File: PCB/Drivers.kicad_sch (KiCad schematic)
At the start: 95 parts, among them U10 TMC2209-LA-T, U11 TMC2209-LA-T, U5 TMC2209-LA-T, U6 ISO1042DWVR, U7 TMC2209-LA-T, U8 TMC2209-LA-T, U9 TMC2209-LA-T

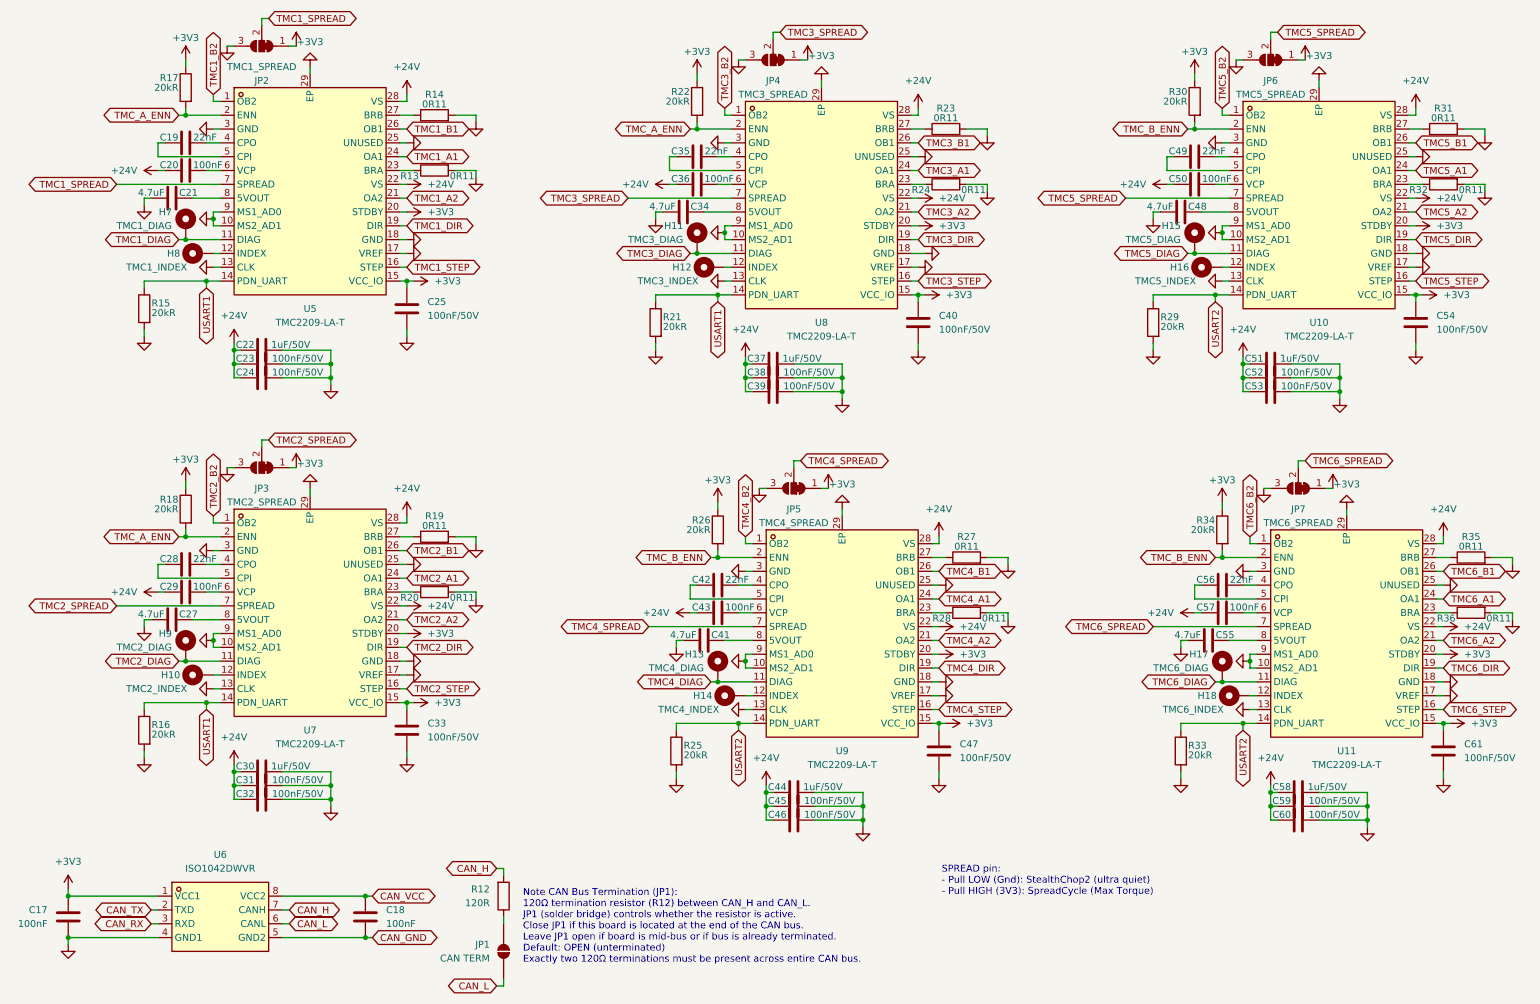
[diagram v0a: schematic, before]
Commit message: Improved Protection and Board Testability - Added power rail protection and decoupling for stepper motor noise environment - Added TVS, bulk caps and fuse upgrade on 24V rail - Added test pads for bring-up and debugging
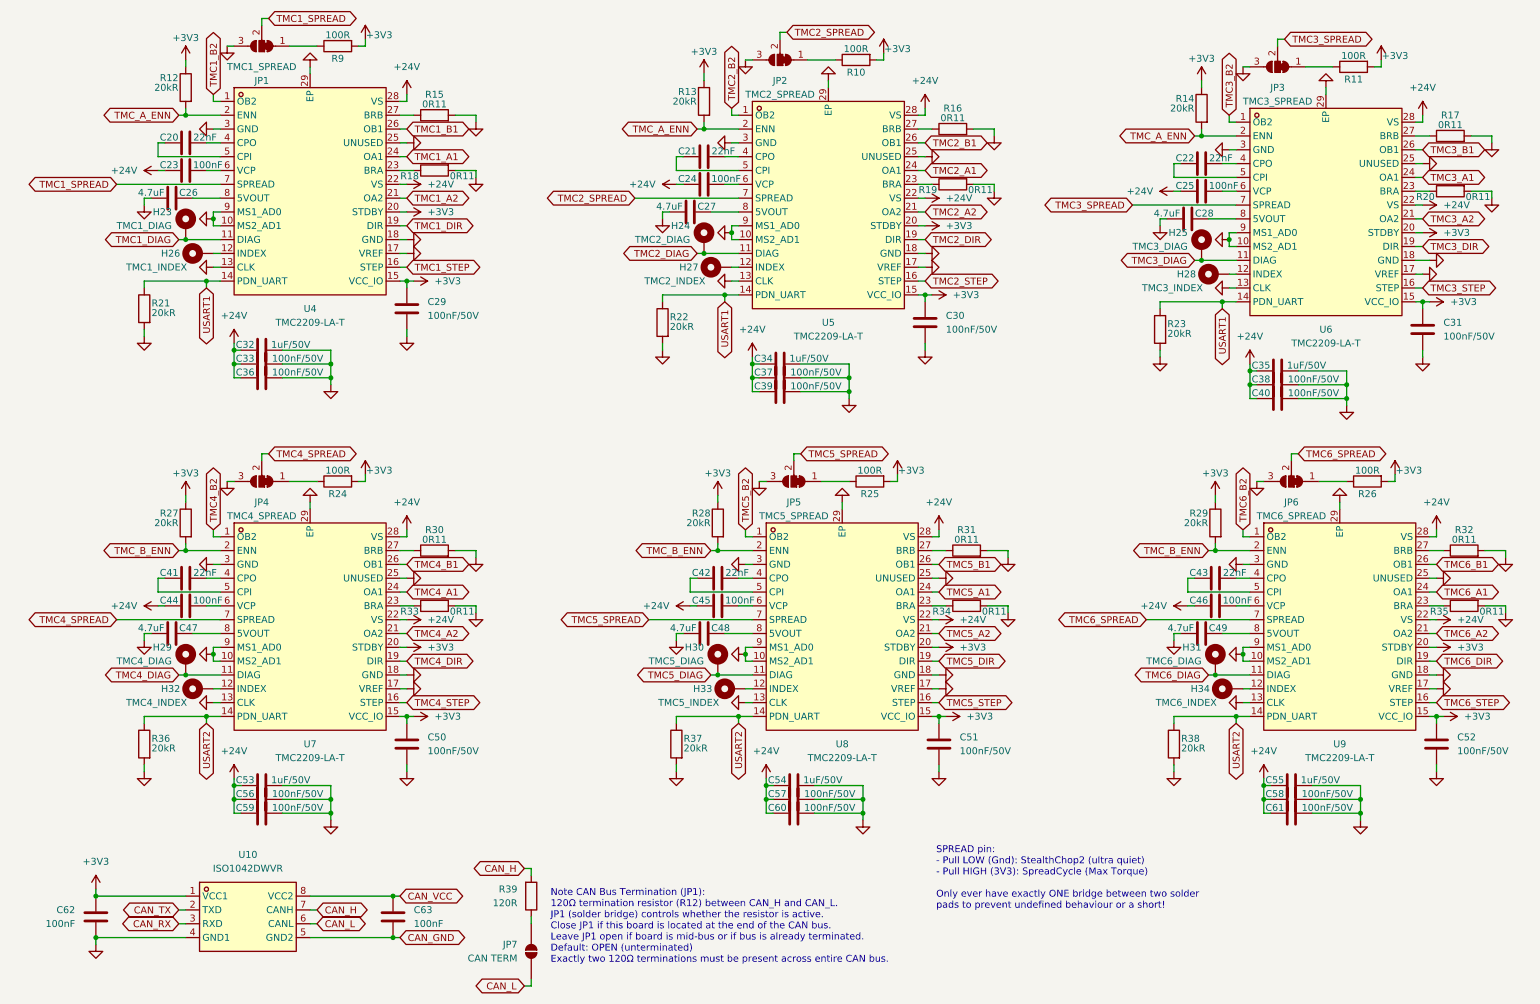
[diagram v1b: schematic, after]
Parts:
- added R10, R11, R24, R25, R26, R9: 100R, Resistor_SMD:R_0402_1005Metric, symbol Device:R
- H23: renamed from H7; footprint TestPoint:TestPoint_Pad_D1.5mm -> TestPoint:TestPoint_Pad_D1.0mm
- H24: renamed from H9; footprint TestPoint:TestPoint_Pad_D1.5mm -> TestPoint:TestPoint_Pad_D1.0mm
- H25: renamed from H11; footprint TestPoint:TestPoint_Pad_D1.5mm -> TestPoint:TestPoint_Pad_D1.0mm
- H26: renamed from H8; footprint TestPoint:TestPoint_Pad_D1.5mm -> TestPoint:TestPoint_Pad_D1.0mm
- H27: renamed from H10; footprint TestPoint:TestPoint_Pad_D1.5mm -> TestPoint:TestPoint_Pad_D1.0mm
- H28: renamed from H12; footprint TestPoint:TestPoint_Pad_D1.5mm -> TestPoint:TestPoint_Pad_D1.0mm
- H29: renamed from H13; footprint TestPoint:TestPoint_Pad_D1.5mm -> TestPoint:TestPoint_Pad_D1.0mm
- H30: renamed from H15; footprint TestPoint:TestPoint_Pad_D1.5mm -> TestPoint:TestPoint_Pad_D1.0mm
- H31: renamed from H17; footprint TestPoint:TestPoint_Pad_D1.5mm -> TestPoint:TestPoint_Pad_D1.0mm
- H32: renamed from H14; footprint TestPoint:TestPoint_Pad_D1.5mm -> TestPoint:TestPoint_Pad_D1.0mm
- H33: renamed from H16; footprint TestPoint:TestPoint_Pad_D1.5mm -> TestPoint:TestPoint_Pad_D1.0mm
- H34: renamed from H18; footprint TestPoint:TestPoint_Pad_D1.5mm -> TestPoint:TestPoint_Pad_D1.0mm
- renumbered C19 to C20, C28 to C21, C35 to C22, C20 to C23, C29 to C24, C36 to C25, C21 to C26, C34 to C28, C25 to C29, C33 to C30, C40 to C31, C22 to C32, C23 to C33, C30 to C34, C37 to C35, C24 to C36, C31 to C37, C32 to C39, C39 to C40, C42 to C41, C49 to C42, C56 to C43, C43 to C44, C50 to C45, C57 to C46, C41 to C47, C55 to C49, C47 to C50, C54 to C51, C61 to C52, C44 to C53, C51 to C54, C58 to C55, C45 to C56, C52 to C57, C59 to C58, C46 to C59, C53 to C60, C60 to C61, C17 to C62, C18 to C63, JP2 to JP1, JP3 to JP2, JP4 to JP3, JP5 to JP4, JP6 to JP5, JP7 to JP6, JP1 to JP7, R17 to R12, R18 to R13, R22 to R14, R14 to R15, R19 to R16, R23 to R17, R13 to R18, R20 to R19, R24 to R20, R15 to R21, R16 to R22, R21 to R23, R26 to R27, R30 to R28, R34 to R29, R27 to R30, R35 to R32, R28 to R33, R32 to R34, R36 to R35, R25 to R36, R29 to R37, R33 to R38, R12 to R39, U6 to U10, U5 to U4, U7 to U5, U8 to U6, U9 to U7, U10 to U8, U11 to U9
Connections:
- net +3V3: now also R10.2, R11.2, R24.2, R25.2, R26.2, R9.2; no longer JP1.1 (A), JP2.1 (A), JP3.1 (A), JP4.1 (A), JP5.1 (A), JP6.1 (A)
- new net: JP4.1 (A), R24.1
- new net: JP1.1 (A), R9.1
- new net: JP2.1 (A), R10.1
- new net: JP6.1 (A), R26.1
- new net: JP3.1 (A), R11.1
- new net: JP5.1 (A), R25.1
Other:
- note added: "SPREAD pin: - Pull LOW (Gnd): StealthChop2 (ultra quiet) - Pull HIGH (3V3): SpreadCycle (Max Torque) Only ever have exactly ONE bridge between two solder pads to prevent undefined behaviour or a short!"
- note removed: "SPREAD pin: - Pull LOW (Gnd): StealthChop2 (ultra quiet) - Pull HIGH (3V3): SpreadCycle (Max Torque)"
- moved on the sheet: C21, C22, C24, C25, C27, C28, C30, C31, C34, C35, C37, C38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

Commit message: PCB Layout: Initial TMC2209 driver cluster layout
- Defined netclasses for 24V, Stepper Motor, 3V3, 5V and Signal
- Decided on 4-layer stackup: Signal / GND / Power / Signal
- Routed high current motor output traces with tapered zone fills
- Placed and routed VS decoupling caps (100nF, 1uF, 47uF electrolytic)
- Routed sense resistors with dedicated GND vias per resistor
- Routed BRA/BRB via bottom layer with perpendicular crossing under motor traces
- Planned +24V / +3V3 split power plane on L3
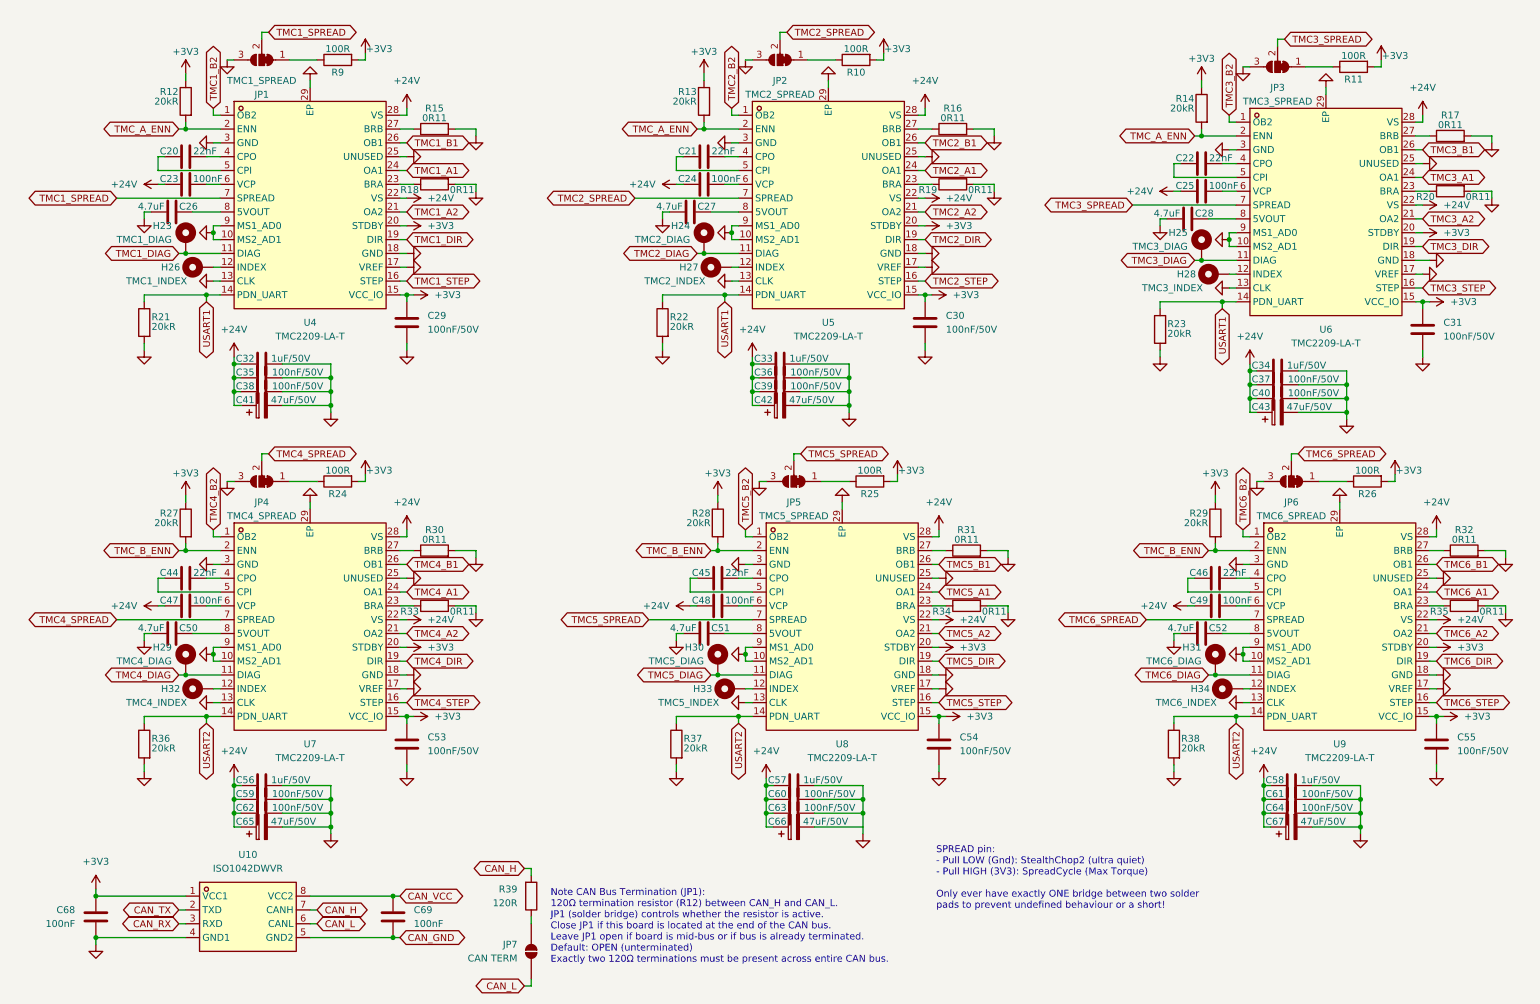
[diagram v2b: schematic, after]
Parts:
- added C41, C42, C43, C65, C66, C67: 47uF/50V, Capacitor_SMD:CP_Elec_8x10.5, symbol Device:C_Polarized
- renumbered C34 to C33, C35 to C34, C33 to C35, C37 to C36, C38 to C37, C36 to C38, C41 to C44, C42 to C45, C43 to C46, C44 to C47, C45 to C48, C46 to C49, C47 to C50, C48 to C51, C49 to C52, C50 to C53, C51 to C54, C52 to C55, C53 to C56, C54 to C57, C55 to C58, C56 to C59, C57 to C60, C58 to C61, C59 to C62, C60 to C63, C61 to C64, C62 to C68, C63 to C69
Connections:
- net +24V: now also C41.1, C42.1, C43.1, C65.1, C66.1, C67.1
- net GND: now also C41.2, C42.2, C43.2, C65.2, C67.2
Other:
- moved on the sheet: C20, C23, C26, C29, C32, C35, C38, H23, H26, JP1, R12, R15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

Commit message: Started laying out the PCB - Decided for a square-shaped board - Split Motor Controllers on top and bottom - Split Power Plane (+3V3 on logic side, +24V on motor side) - Roughly layed out the board entirely - Reconsidered my life choises (got sick)
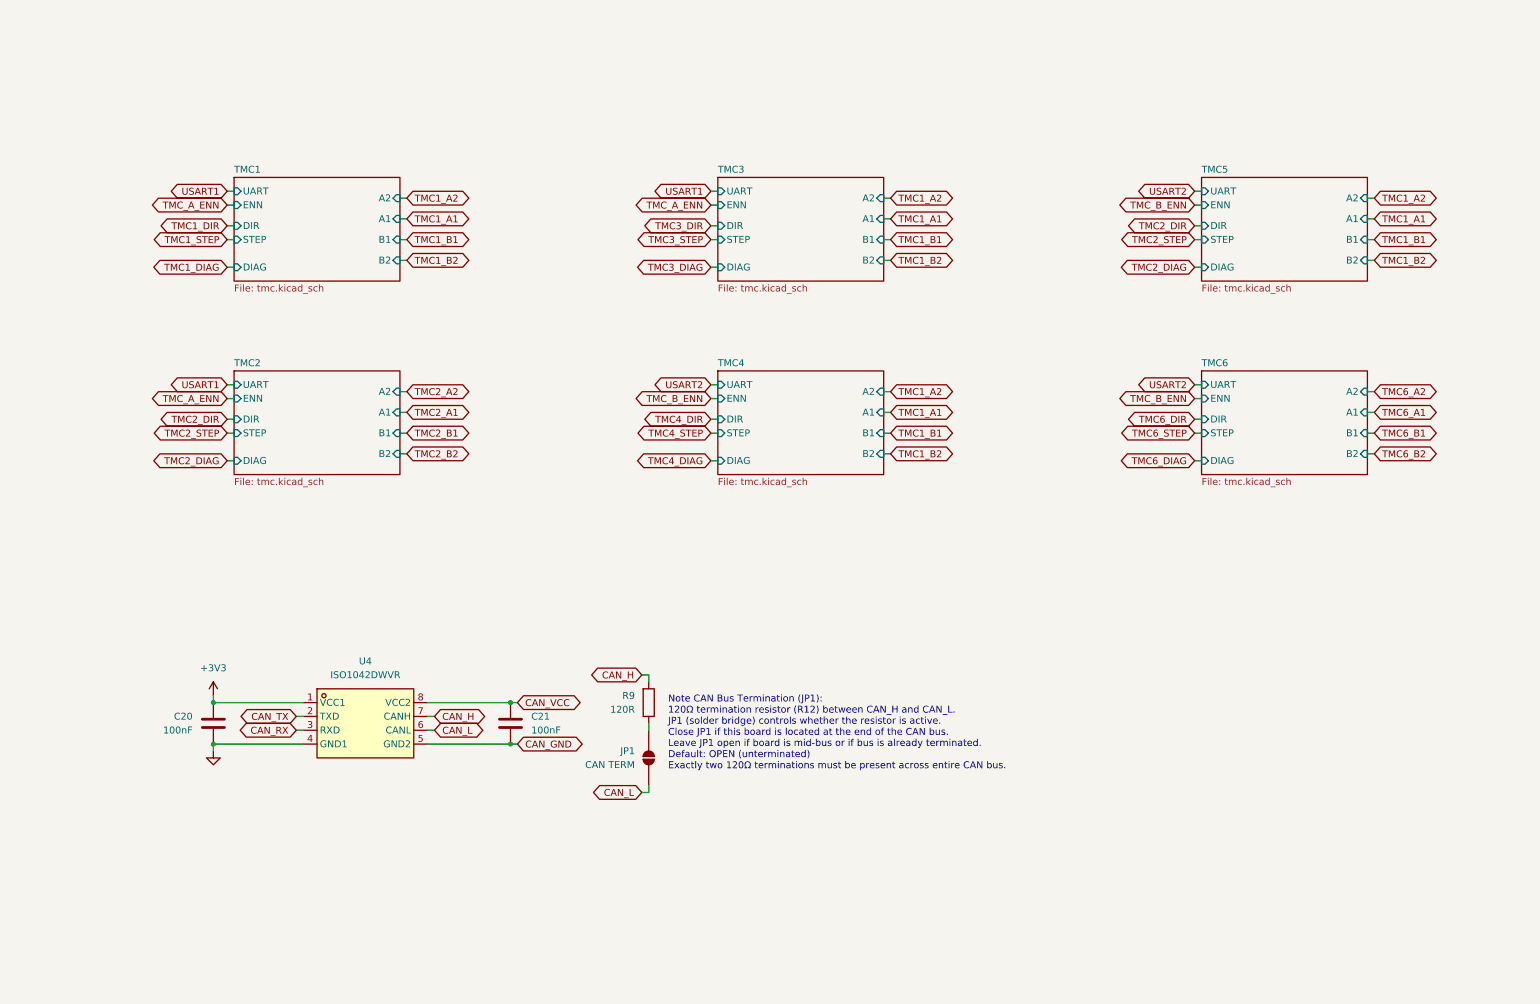
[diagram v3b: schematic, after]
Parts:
- removed C20, C21, C22, C44, C45, C46: 22nF, Capacitor_SMD:C_0402_1005Metric, symbol Device:C
- removed C23, C24, C25, C47, C48, C49: 100nF, Capacitor_SMD:C_0402_1005Metric, symbol Device:C
- removed C26, C27, C28, C50, C51, C52: 4.7uF, Capacitor_SMD:C_0805_2012Metric, symbol Device:C
- removed C29, C30, C31, C35, C36, C37, C38, C39, C40, C53, C54, C55, C59, C60, C61, C62, C63, C64: 100nF/50V, Capacitor_SMD:C_0402_1005Metric, symbol Device:C
- removed C32, C33, C34, C56, C57: 1uF/50V, Capacitor_SMD:C_0603_1608Metric, symbol Device:C
- removed C41, C42, C43, C65, C66, C67: 47uF/50V, Capacitor_SMD:CP_Elec_8x10.5, symbol Device:C_Polarized
- removed C58: 1uF/50V, Capacitor_SMD:C_0805_2012Metric, symbol Device:C
- removed H23: TMC1_DIAG, TestPoint:TestPoint_Pad_D1.0mm, symbol Mechanical:MountingHole_Pad
- removed H24: TMC2_DIAG, TestPoint:TestPoint_Pad_D1.0mm, symbol Mechanical:MountingHole_Pad
- removed H25: TMC3_DIAG, TestPoint:TestPoint_Pad_D1.0mm, symbol Mechanical:MountingHole_Pad
- removed H26: TMC1_INDEX, TestPoint:TestPoint_Pad_D1.0mm, symbol Mechanical:MountingHole_Pad
- removed H27: TMC2_INDEX, TestPoint:TestPoint_Pad_D1.0mm, symbol Mechanical:MountingHole_Pad
- removed H28: TMC3_INDEX, TestPoint:TestPoint_Pad_D1.0mm, symbol Mechanical:MountingHole_Pad
- removed H29: TMC4_DIAG, TestPoint:TestPoint_Pad_D1.0mm, symbol Mechanical:MountingHole_Pad
- removed H30: TMC5_DIAG, TestPoint:TestPoint_Pad_D1.0mm, symbol Mechanical:MountingHole_Pad
- removed H31: TMC6_DIAG, TestPoint:TestPoint_Pad_D1.0mm, symbol Mechanical:MountingHole_Pad
- removed H32: TMC4_INDEX, TestPoint:TestPoint_Pad_D1.0mm, symbol Mechanical:MountingHole_Pad
- removed H33: TMC5_INDEX, TestPoint:TestPoint_Pad_D1.0mm, symbol Mechanical:MountingHole_Pad
- removed H34: TMC6_INDEX, TestPoint:TestPoint_Pad_D1.0mm, symbol Mechanical:MountingHole_Pad
- removed JP1: TMC1_SPREAD, Jumper:SolderJumper-3_P1.3mm_Bridged2Bar12_RoundedPad1.0x1.5mm, symbol Jumper:SolderJumper_3_Bridged12
- removed JP2: TMC2_SPREAD, Jumper:SolderJumper-3_P1.3mm_Bridged2Bar12_RoundedPad1.0x1.5mm, symbol Jumper:SolderJumper_3_Bridged12
- removed JP3: TMC3_SPREAD, Jumper:SolderJumper-3_P1.3mm_Bridged2Bar12_RoundedPad1.0x1.5mm, symbol Jumper:SolderJumper_3_Bridged12
- removed JP4: TMC4_SPREAD, Jumper:SolderJumper-3_P1.3mm_Bridged2Bar12_RoundedPad1.0x1.5mm, symbol Jumper:SolderJumper_3_Bridged12
- removed JP5: TMC5_SPREAD, Jumper:SolderJumper-3_P1.3mm_Bridged2Bar12_RoundedPad1.0x1.5mm, symbol Jumper:SolderJumper_3_Bridged12
- removed JP6: TMC6_SPREAD, Jumper:SolderJumper-3_P1.3mm_Bridged2Bar12_RoundedPad1.0x1.5mm, symbol Jumper:SolderJumper_3_Bridged12
- removed R10, R11, R24, R25, R26, R9: 100R, Resistor_SMD:R_0402_1005Metric, symbol Device:R
- removed R12, R13, R14, R21, R22, R23, R27, R28, R29, R36, R37, R38: 20kR, Resistor_SMD:R_0402_1005Metric, symbol Device:R
- removed R15, R16, R17, R18, R19, R20, R30, R31, R32, R33, R34, R35: 0R11, Resistor_SMD:R_1206_3216Metric, symbol Device:R
- removed U4, U5, U6, U7, U8, U9: TMC2209-LA-T, lcsc:QFN-28_L5.0-W5.0-P0.50-BL-EP, symbol lcsc:TMC2209-LA-T
- renumbered C68 to C20, C69 to C21, JP7 to JP1, R39 to R9, U10 to U4
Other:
- added sheet TMC1 (tmc.kicad_sch)
- added sheet TMC2 (tmc.kicad_sch)
- added sheet TMC3 (tmc.kicad_sch)
- added sheet TMC4 (tmc.kicad_sch)
- added sheet TMC5 (tmc.kicad_sch)
- added sheet TMC6 (tmc.kicad_sch)
- note removed: "SPREAD pin: - Pull LOW (Gnd): StealthChop2 (ultra quiet) - Pull HIGH (3V3): SpreadCycle (Max Torque) Only ever have exactly ONE bridge between two solder pads to prevent undefined behaviour or a short!"
- moved on the sheet: C20, C21, JP1, R9, U4
